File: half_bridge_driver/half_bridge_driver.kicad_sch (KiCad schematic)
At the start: 64 parts, among them CN1 X3025WVS-2*10D-LPSW, IC2 AMC1311BDWV, J11 Conn_02x10_Top_Bottom, J7 Conn_01x06_Pin, Q12 ${MANUFACTURER PART}, Q15 SN74ACT244PWRG4, Q3 ${MANUFACTURER PART}, U1 K78U12, U2 ISO7340C, U3 ISO7340C

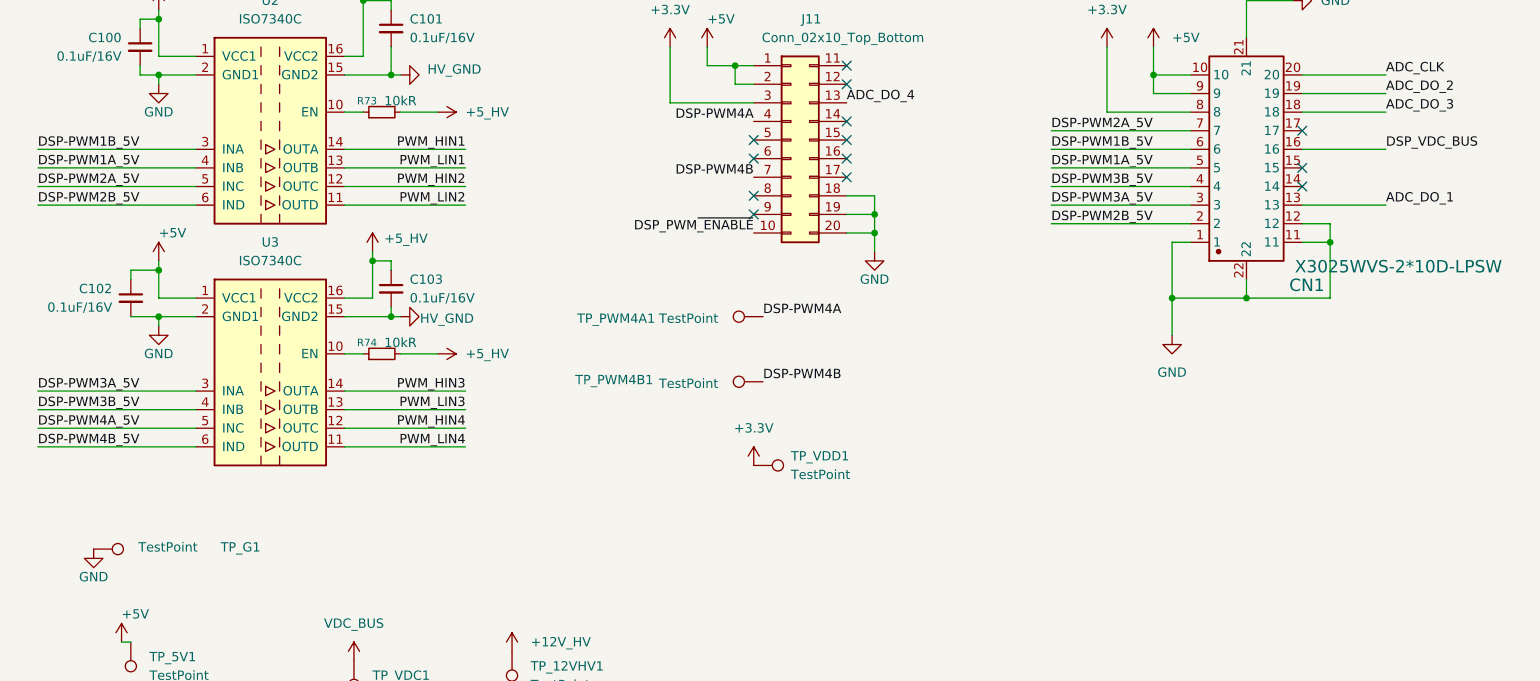
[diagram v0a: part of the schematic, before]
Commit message: 修改了half bridge的PWM 反了的bug
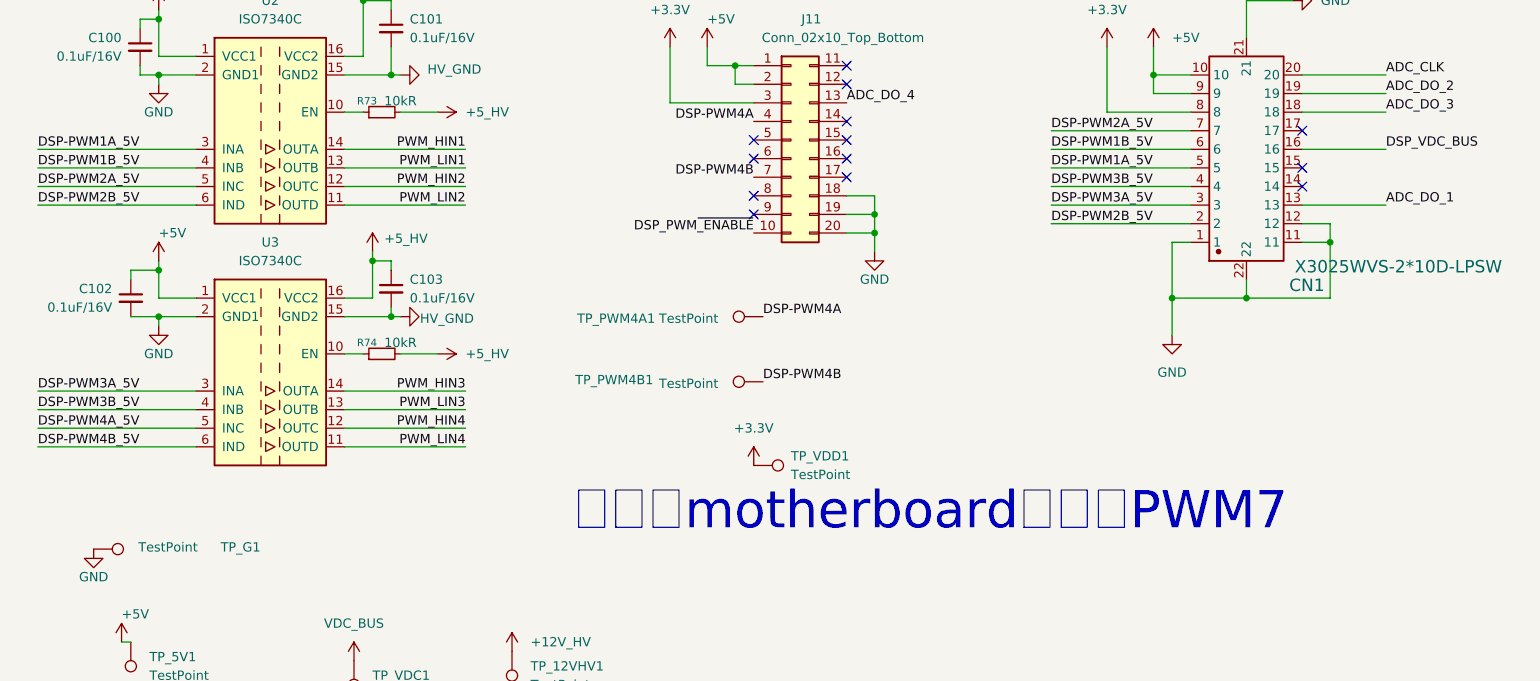
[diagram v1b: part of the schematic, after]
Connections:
- net DSP-PWM1A_5V: now also U2.3 (INA); no longer U2.4 (INB)
- net DSP-PWM1B_5V: now also U2.4 (INB); no longer U2.3 (INA)
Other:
- note added: "对应到motherboard其实是PWM7"
